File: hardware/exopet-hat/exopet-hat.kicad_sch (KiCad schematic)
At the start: 47 parts, among them J1 12V DC in, J10 CH3 12V OUT, J11 CH4 dry contact, J12 EZO side B (RX/PRB), J2 12V screw term, J3 RPi GPIO (HAT), J4 DS18B20 TRS jack, J5 DS18B20 JST, J6 BNC pH probe, J7 EZO side A (VCC/GND/TX), J8 CH1 12V OUT, J9 CH2 12V OUT, K1 G5LE-1 DC12, K2 G5LE-1 DC12, K3 G5LE-1 DC12, K4 G5LE-1 DC12, Q1 DMP4015SK3, U2 TBD62003APG, U4 CAT24C32, U5 TPD1E10B06

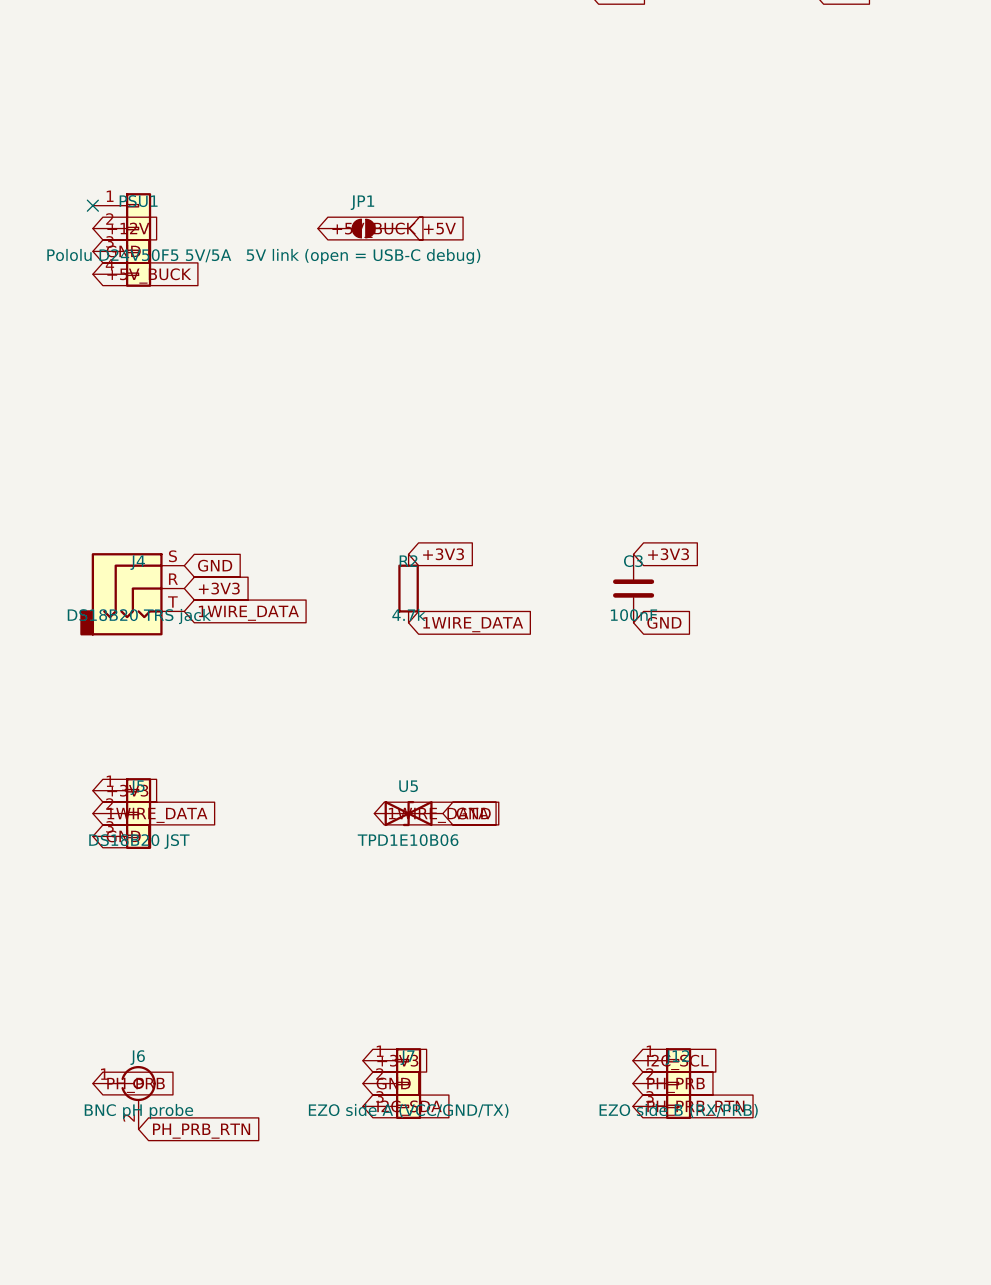
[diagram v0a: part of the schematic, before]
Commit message: Verify HAT schematic against datasheets; fix EZO pinout and buck socket
- EZO-pH socket regrouped per Atlas datasheet v6.1 (GND/TX/RX top,
  VCC/PRB/PGND bottom) — original grouping was wrong
- Pololu D24V50F5 socket corrected from 4 to 5 pins (EN/VIN/2xGND/VOUT)
- G5LE-1 relay mapping confirmed against Omron datasheet (coil 2/5,
  COM 1, NO 3, NC 4)
- README documents verification and Atlas's pH isolation warning for
  commercial boards (rev 2 requirement)

Co-Authored-By: Claude Fable 5 <noreply@anthropic.com>
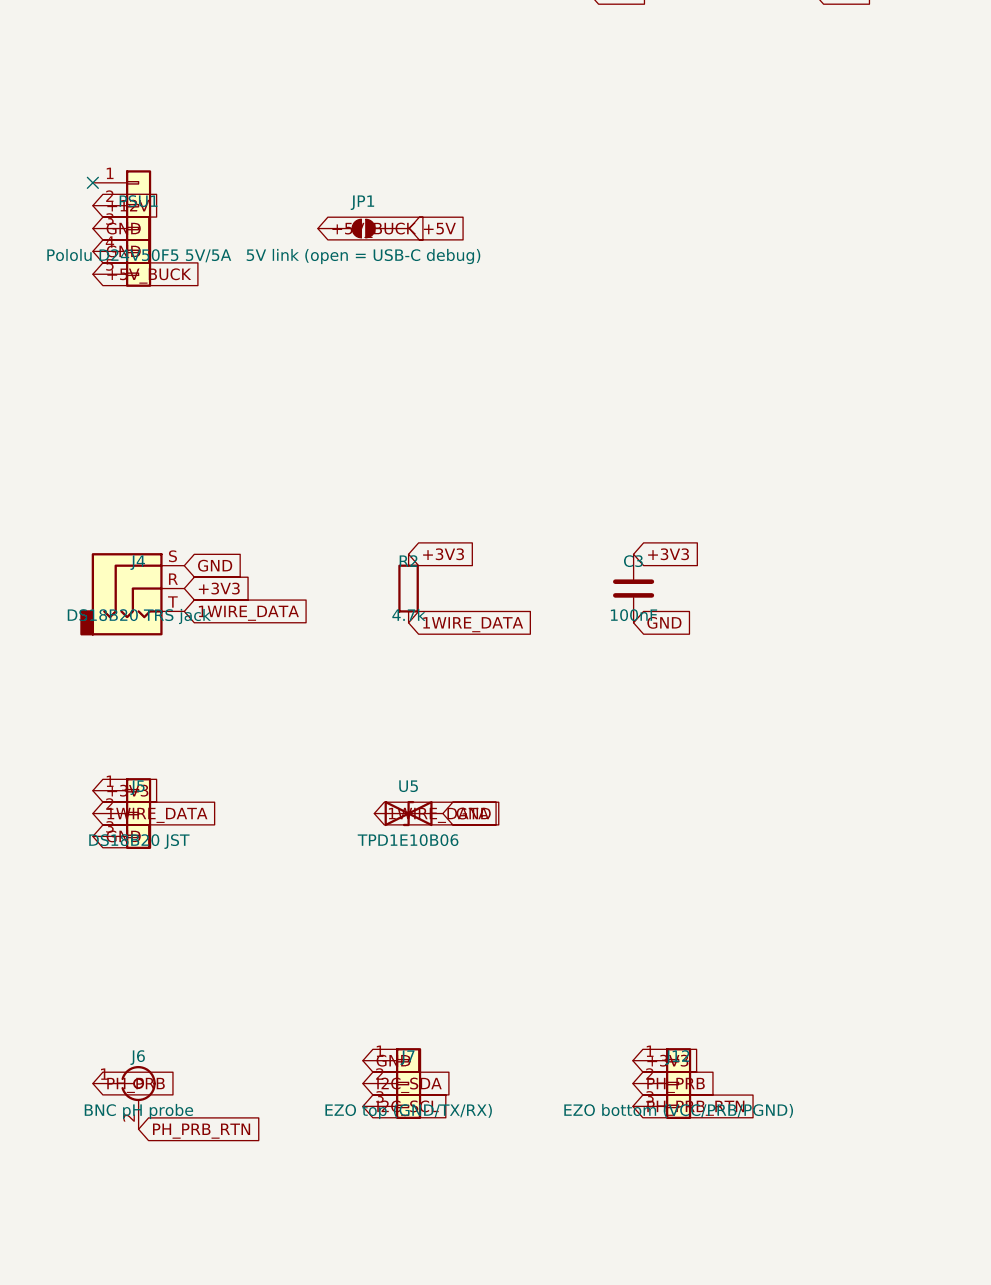
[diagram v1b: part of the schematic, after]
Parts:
- J12: value EZO side B (RX/PRB) -> EZO bottom (VCC/PRB/PGND)
- J7: value EZO side A (VCC/GND/TX) -> EZO top (GND/TX/RX)
- PSU1: symbol Connector_Generic:Conn_01x04 -> Connector_Generic:Conn_01x05
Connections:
- net +3V3: now also J12.1 (Pin_1); no longer J7.1 (Pin_1)
- net +5V_BUCK: now also PSU1.5 (Pin_5); no longer PSU1.4 (Pin_4)
- net GND: now also J7.1 (Pin_1), PSU1.4 (Pin_4); no longer J7.2 (Pin_2)
- net I2C_SCL: now also J7.3 (Pin_3); no longer J12.1 (Pin_1)
- net I2C_SDA: now also J7.2 (Pin_2); no longer J7.3 (Pin_3)
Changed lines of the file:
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@@
     )
   )
-  (symbol (lib_id "Connector_Generic:Conn_01x04") (at 30 90 0) (unit 1)
+  (symbol (lib_id "Connector_Generic:Conn_01x05") (at 30 90 0) (unit 1)
     (exclude_from_sim no) (in_bom yes) (on_board yes) (dnp no)
     (property "Reference" "PSU1" (at 30 87 0) (effects (font (size 1.27 1.27))))
@@
     (pin "3")
     (pin "4")
+    (pin "5")
     (instances
       (project "exopet-hat"
@@
     (exclude_from_sim no) (in_bom yes) (on_board yes) (dnp no)
     (property "Reference" "J7" (at 60 182 0) (effects (font (size 1.27 1.27))))
-    (property "Value" "EZO side A (VCC/GND/TX)" (at 60 188 0) (effects (font (size 1.27 1.27))))
+    (property "Value" "EZO top (GND/TX/RX)" (at 60 188 0) (effects (font (size 1.27 1.27))))
     (property "Footprint" "" (at 60 185 0) (effects (font (size 1.27 1.27)) hide))
     (pin "1")
@@
     (exclude_from_sim no) (in_bom yes) (on_board yes) (dnp no)
     (property "Reference" "J12" (at 90 182 0) (effects (font (size 1.27 1.27))))
-    (property "Value" "EZO side B (RX/PRB)" (at 90 188 0) (effects (font (size 1.27 1.27))))
+    (property "Value" "EZO bottom (VCC/PRB/PGND)" (at 90 188 0) (effects (font (size 1.27 1.27))))
     (property "Footprint" "" (at 90 185 0) (effects (font (size 1.27 1.27)) hide))
     (pin "1")
@@
   (global_label "+12V" (shape input) (at 105.0 56.19 0) (effects (font (size 1.27 1.27)) (justify left)))
   (global_label "GND" (shape input) (at 105.0 63.81 0) (effects (font (size 1.27 1.27)) (justify left)))
-  (global_label "+12V" (shape input) (at 24.92 90.0 0) (effects (font (size 1.27 1.27)) (justify left)))
+  (global_label "+12V" (shape input) (at 24.92 87.46 0) (effects (font (size 1.27 1.27)) (justify left)))
+  (global_label "GND" (shape input) (at 24.92 90.0 0) (effects (font (size 1.27 1.27)) (justify left)))
   (global_label "GND" (shape input) (at 24.92 92.54 0) (effects (font (size 1.27 1.27)) (justify left)))
   (global_label "+5V_BUCK" (shape input) (at 24.92 95.08 0) (effects (font (size 1.27 1.27)) (justify left)))
@@
   (global_label "PH_PRB" (shape input) (at 24.92 185.0 0) (effects (font (size 1.27 1.27)) (justify left)))
   (global_label "PH_PRB_RTN" (shape input) (at 30.0 190.08 0) (effects (font (size 1.27 1.27)) (justify left)))
-  (global_label "+3V3" (shape input) (at 54.92 182.46 0) (effects (font (size 1.27 1.27)) (justify left)))
-  (global_label "GND" (shape input) (at 54.92 185.0 0) (effects (font (size 1.27 1.27)) (justify left)))
-  (global_label "I2C_SDA" (shape input) (at 54.92 187.54 0) (effects (font (size 1.27 1.27)) (justify left)))
-  (global_label "I2C_SCL" (shape input) (at 84.92 182.46 0) (effects (font (size 1.27 1.27)) (justify left)))
+  (global_label "GND" (shape input) (at 54.92 182.46 0) (effects (font (size 1.27 1.27)) (justify left)))
+  (global_label "I2C_SDA" (shape input) (at 54.92 185.0 0) (effects (font (size 1.27 1.27)) (justify left)))
+  (global_label "I2C_SCL" (shape input) (at 54.92 187.54 0) (effects (font (size 1.27 1.27)) (justify left)))
+  (global_label "+3V3" (shape input) (at 84.92 182.46 0) (effects (font (size 1.27 1.27)) (justify left)))
   (global_label "PH_PRB" (shape input) (at 84.92 185.0 0) (effects (font (size 1.27 1.27)) (justify left)))
   (global_label "PH_PRB_RTN" (shape input) (at 84.92 187.54 0) (effects (font (size 1.27 1.27)) (justify left)))
@@
   (global_label "GND" (shape input) (at 130.0 215.0 0) (effects (font (size 1.27 1.27)) (justify left)))
   (no_connect (at 37.62 40.0))
-  (no_connect (at 24.92 87.46))
+  (no_connect (at 24.92 84.92))
   (no_connect (at 149.68 47.14))
   (no_connect (at 149.68 49.68))

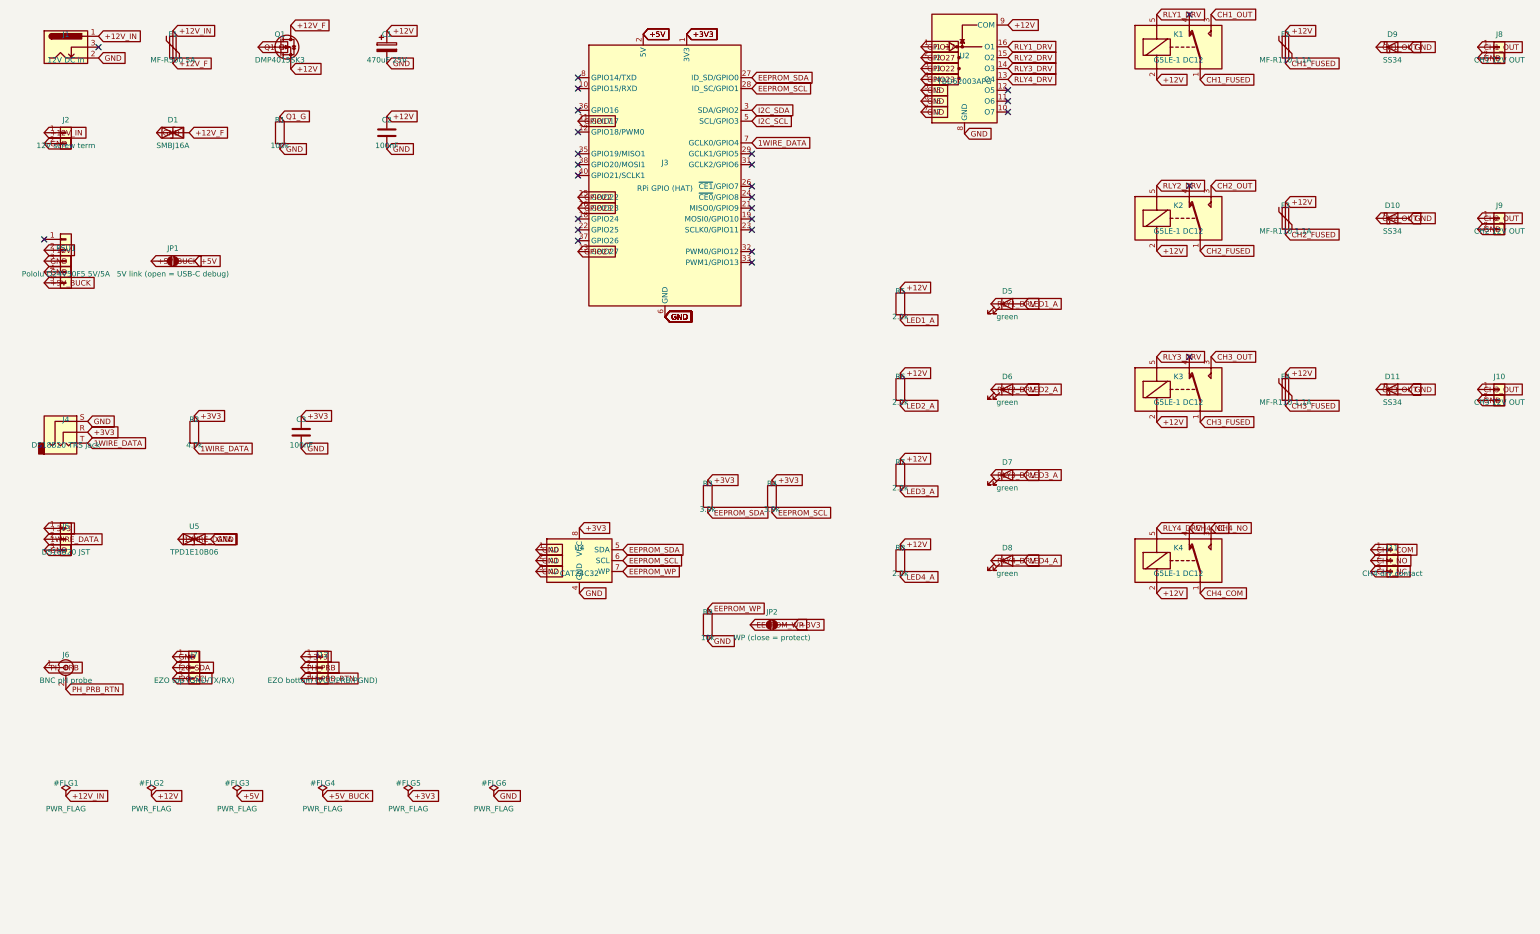
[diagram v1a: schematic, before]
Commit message: Drop pH from HAT rev 1; defer to isolated rev 2 design
Per Atlas EZO-pH datasheet isolation requirements near pumps/valves.
BNC and EZO sockets removed from schematic and preview; GPIO2/3 left
unconnected and reserved. ERC still clean; netlist re-verified with
pH nets and parts confirmed absent, EEPROM path intact.

Co-Authored-By: Claude Fable 5 <noreply@anthropic.com>
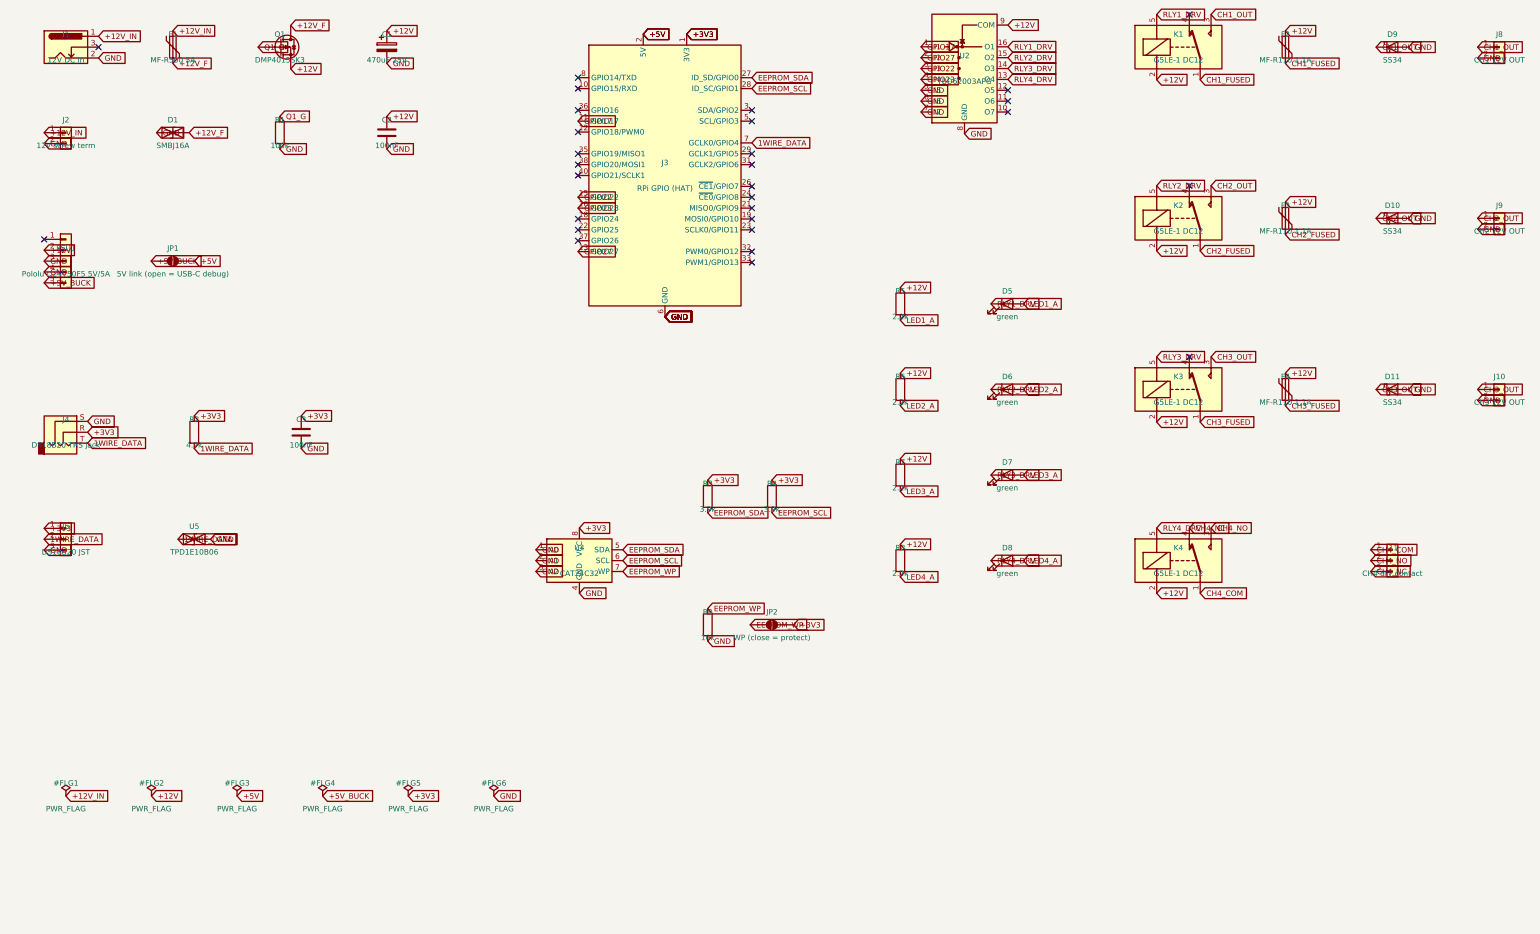
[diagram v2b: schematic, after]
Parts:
- removed J12: EZO bottom (VCC/PRB/PGND), symbol Connector_Generic:Conn_01x03
- removed J6: BNC pH probe, symbol Connector:Conn_Coaxial
- removed J7: EZO top (GND/TX/RX), symbol Connector_Generic:Conn_01x03
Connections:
- net I2C_SCL: no longer names the net of J3.5 (SCL/GPIO3)
- net I2C_SDA: no longer names the net of J3.3 (SDA/GPIO2)
- no-connect marks 27 -> 29
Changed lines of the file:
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@@
-    )
-  )
-  (symbol (lib_id "Connector:Conn_Coaxial") (at 30 185 0) (unit 1)
-    (exclude_from_sim no) (in_bom yes) (on_board yes) (dnp no)
-    (property "Reference" "J6" (at 30 182 0) (effects (font (size 1.27 1.27))))
-    (property "Value" "BNC pH probe" (at 30 188 0) (effects (font (size 1.27 1.27))))
-    (property "Footprint" "" (at 30 185 0) (effects (font (size 1.27 1.27)) hide))
-    (pin "1")
-    (pin "2")
-    (instances
-      (project "exopet-hat"
-        (path "/e0a7e100-0000-4000-8000-00000000c0de" (reference "J6") (unit 1))
-      )
-    )
-  )
-  (symbol (lib_id "Connector_Generic:Conn_01x03") (at 60 185 0) (unit 1)
-    (exclude_from_sim no) (in_bom yes) (on_board yes) (dnp no)
-    (property "Reference" "J7" (at 60 182 0) (effects (font (size 1.27 1.27))))
-    (property "Value" "EZO top (GND/TX/RX)" (at 60 188 0) (effects (font (size 1.27 1.27))))
-    (property "Footprint" "" (at 60 185 0) (effects (font (size 1.27 1.27)) hide))
-    (pin "1")
-    (pin "2")
-    (pin "3")
-    (instances
-      (project "exopet-hat"
-        (path "/e0a7e100-0000-4000-8000-00000000c0de" (reference "J7") (unit 1))
-      )
-    )
-  )
-  (symbol (lib_id "Connector_Generic:Conn_01x03") (at 90 185 0) (unit 1)
-    (exclude_from_sim no) (in_bom yes) (on_board yes) (dnp no)
-    (property "Reference" "J12" (at 90 182 0) (effects (font (size 1.27 1.27))))
-    (property "Value" "EZO bottom (VCC/PRB/PGND)" (at 90 188 0) (effects (font (size 1.27 1.27))))
-    (property "Footprint" "" (at 90 185 0) (effects (font (size 1.27 1.27)) hide))
-    (pin "1")
-    (pin "2")
-    (pin "3")
-    (instances
-      (project "exopet-hat"
-        (path "/e0a7e100-0000-4000-8000-00000000c0de" (reference "J12") (unit 1))
-      )
     )
   )
@@
   (global_label "GND" (shape input) (at 170.0 103.02 0) (effects (font (size 1.27 1.27)) (justify left)))
   (global_label "GND" (shape input) (at 170.0 103.02 0) (effects (font (size 1.27 1.27)) (justify left)))
-  (global_label "I2C_SDA" (shape input) (at 190.32 54.76 0) (effects (font (size 1.27 1.27)) (justify left)))
-  (global_label "I2C_SCL" (shape input) (at 190.32 57.3 0) (effects (font (size 1.27 1.27)) (justify left)))
   (global_label "1WIRE_DATA" (shape input) (at 190.32 62.38 0) (effects (font (size 1.27 1.27)) (justify left)))
   (global_label "GPIO17" (shape input) (at 149.68 57.3 0) (effects (font (size 1.27 1.27)) (justify left)))
@@
   (global_label "+3V3" (shape input) (at 85.0 126.19 0) (effects (font (size 1.27 1.27)) (justify left)))
   (global_label "GND" (shape input) (at 85.0 133.81 0) (effects (font (size 1.27 1.27)) (justify left)))
-  (global_label "PH_PRB" (shape input) (at 24.92 185.0 0) (effects (font (size 1.27 1.27)) (justify left)))
-  (global_label "PH_PRB_RTN" (shape input) (at 30.0 190.08 0) (effects (font (size 1.27 1.27)) (justify left)))
-  (global_label "GND" (shape input) (at 54.92 182.46 0) (effects (font (size 1.27 1.27)) (justify left)))
-  (global_label "I2C_SDA" (shape input) (at 54.92 185.0 0) (effects (font (size 1.27 1.27)) (justify left)))
-  (global_label "I2C_SCL" (shape input) (at 54.92 187.54 0) (effects (font (size 1.27 1.27)) (justify left)))
-  (global_label "+3V3" (shape input) (at 84.92 182.46 0) (effects (font (size 1.27 1.27)) (justify left)))
-  (global_label "PH_PRB" (shape input) (at 84.92 185.0 0) (effects (font (size 1.27 1.27)) (justify left)))
-  (global_label "PH_PRB_RTN" (shape input) (at 84.92 187.54 0) (effects (font (size 1.27 1.27)) (justify left)))
   (global_label "GND" (shape input) (at 139.84 157.46 0) (effects (font (size 1.27 1.27)) (justify left)))
   (global_label "GND" (shape input) (at 139.84 160.0 0) (effects (font (size 1.27 1.27)) (justify left)))
@@
   (no_connect (at 37.62 40.0))
   (no_connect (at 24.92 84.92))
+  (no_connect (at 190.32 54.76))
+  (no_connect (at 190.32 57.3))
   (no_connect (at 149.68 47.14))
   (no_connect (at 149.68 49.68))
